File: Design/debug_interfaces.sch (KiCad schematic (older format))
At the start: 2 parts, among them J1 Conn_ARM_JTAG_SWD_10, U4 UART_female

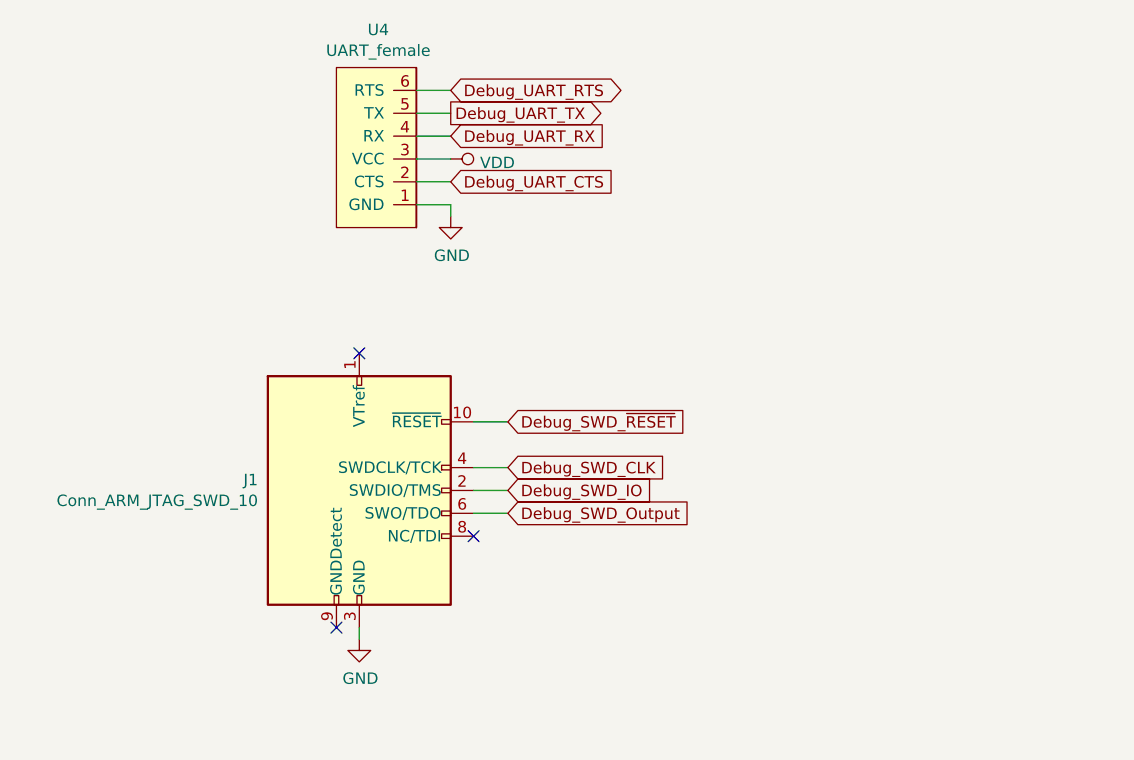
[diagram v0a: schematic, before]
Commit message: Improvement over the Power management: - added TPS6201DRC for raising leaking voltage from supercapacitor - supercap is protected from overvoltage using a shunt diode - power management is using MOSFET logic (2 PFET, 1 NFET)
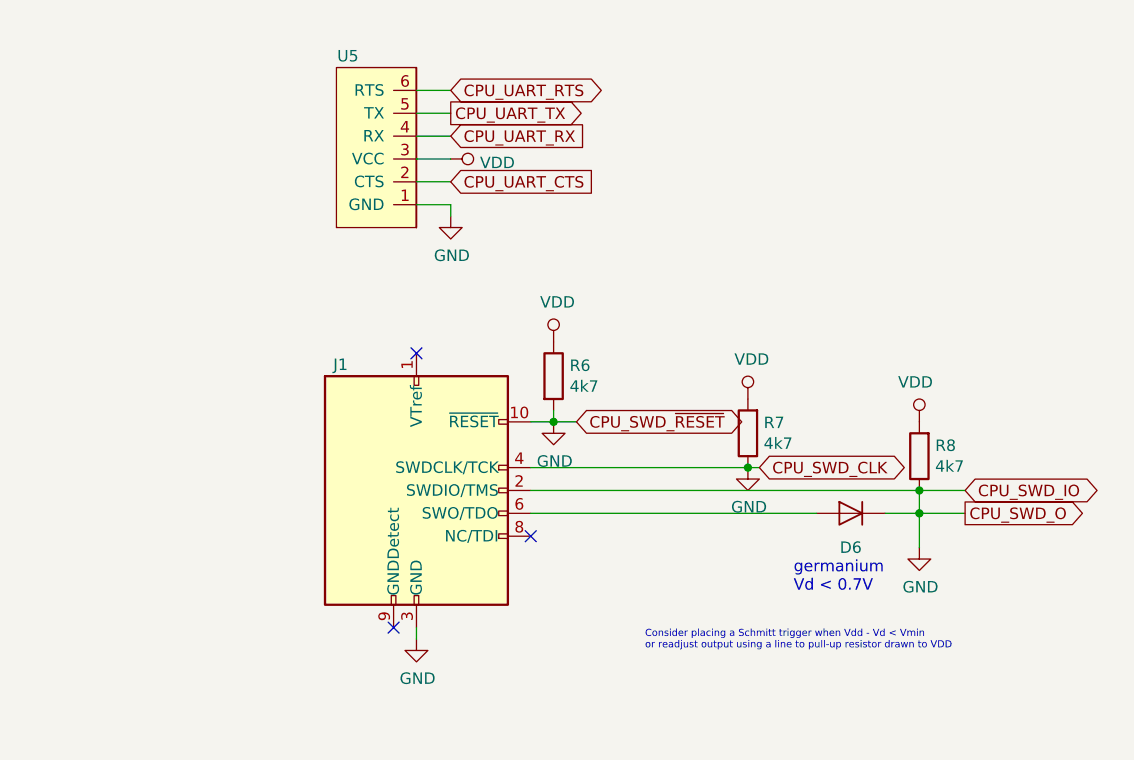
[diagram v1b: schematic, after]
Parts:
- added D6: 1N4148, Diode_THT:D_DO-35_SOD27_P7.62mm_Horizontal, symbol Diode:1N4148
- added R6, R7, R8: 4k7, symbol Device:R
- J1: footprint (none) -> Connector_PinHeader_1.27mm:PinHeader_1x06_P1.27mm_Horizontal
- renumbered U4 to U5
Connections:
- net Debug_SWD_CLK is gone; now on net GND: J1.4 (SWDCLK/TCK)
- net Debug_SWD_IO is gone; now on net GND: J1.2 (SWDIO/TMS)
- net Debug_SWD_~RESET~ is gone; now on net GND: J1.10 (~RESET~)
- net GND: now also D6.1 (K), R6.2, R7.1, R8.1
- net VDD: now also R6.1, R7.2, R8.2
- net Debug_SWD_Output: no longer names the net of J1.6 (SWO/TDO)
- net Debug_SWD_Output: now also D6.2 (A)
- net Debug_UART_CTS renamed CPU_UART_CTS
- net Debug_UART_RTS renamed CPU_UART_RTS
- net Debug_UART_RX renamed CPU_UART_RX
- net Debug_UART_TX renamed CPU_UART_TX
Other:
- note added: "Consider placing a Schmitt trigger when Vdd - Vd < Vmin \nor readjust output using a line to pull-up resistor drawn to VDD"
- note added: "germanium\nVd < 0.7V"
- moved on the sheet: J1
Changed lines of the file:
@@
 L Connector:Conn_ARM_JTAG_SWD_10 J1
 U 1 1 5E1B4BA0
-P 2150 2900
-F 0 "J1" H 1707 2946 50  0000 R CNN
-F 1 "Conn_ARM_JTAG_SWD_10" H 1707 2855 50  0000 R CNN
-F 2 "" H 2150 2900 50  0001 C CNN
-F 3 "http://infocenter.arm.com/help/topic/com.arm.doc.ddi0314h/DDI0314H_coresight_components_trm.pdf" V 1800 1650 50  0001 C CNN
-	1    2150 2900
-	1    0    0    -1
-$EndComp
-$Comp
-L Meishi:UART_female U4
+P 2400 2900
+F 0 "J1" H 2100 3450 50  0000 R CNN
+F 1 "Conn_ARM_JTAG_SWD_10" H 1957 2855 50  0001 R CNN
+F 2 "Connector_PinHeader_1.27mm:PinHeader_1x06_P1.27mm_Horizontal" H 2400 2900 50  0001 C CNN
+F 3 "http://infocenter.arm.com/help/topic/com.arm.doc.ddi0314h/DDI0314H_coresight_components_trm.pdf" V 2050 1650 50  0001 C CNN
+	1    2400 2900
+	1    0    0    -1
+$EndComp
+$Comp
+L Meishi:UART_female U5
 U 1 1 5E1B45D1
 P 2400 1650
-F 0 "U4" H 2567 885 50  0000 C CNN
-F 1 "UART_female" H 2567 976 50  0000 C CNN
+F 0 "U5" H 2700 1000 50  0000 C CNN
+F 1 "UART_female" H 2567 976 50  0001 C CNN
 F 2 "Connector_PinSocket_1.00mm:PinSocket_1x06_P1.00mm_Vertical" H 2800 1100 50  0001 C CNN
 F 3 "" H 2800 1100 50  0001 C CNN
@@
 $EndComp
 $Comp
-L power:GND #PWR0101
+L power:GND #PWR017
 U 1 1 5E1B6C8F
 P 2550 1700
-F 0 "#PWR0101" H 2550 1450 50  0001 C CNN
+F 0 "#PWR017" H 2550 1450 50  0001 C CNN
 F 1 "GND" H 2555 1527 50  0000 C CNN
 F 2 "" H 2550 1700 50  0001 C CNN
@@
 Wire Wire Line
 	2550 1650 2400 1650
-Text GLabel 2550 1250 2    50   Output ~ 0
-Debug_UART_TX
 Wire Wire Line
 	2550 1250 2400 1250
 Text GLabel 2550 1350 2    50   Input ~ 0
-Debug_UART_RX
+CPU_UART_RX
 Wire Wire Line
 	2550 1350 2400 1350
 Text GLabel 2550 1150 2    50   BiDi ~ 0
-Debug_UART_RTS
+CPU_UART_RTS
 Wire Wire Line
 	2550 1150 2400 1150
 Text GLabel 2550 1550 2    50   Input ~ 0
-Debug_UART_CTS
+CPU_UART_CTS
 Wire Wire Line
 	2550 1550 2400 1550
@@
 	2400 1450 2550 1450
 $Comp
-L power:VDD #PWR0102
+L power:VDD #PWR016
 U 1 1 5E1B7012
 P 2550 1450
-F 0 "#PWR0102" H 2550 1300 50  0001 C CNN
+F 0 "#PWR016" H 2550 1300 50  0001 C CNN
 F 1 "VDD" V 2567 1578 50  0000 L CNN
 F 2 "" H 2550 1450 50  0001 C CNN
@@
 $EndComp
 $Comp
-L power:GND #PWR0104
+L power:GND #PWR015
 U 1 1 5E1BD15F
-P 2150 3550
-F 0 "#PWR0104" H 2150 3300 50  0001 C CNN
-F 1 "GND" H 2155 3377 50  0000 C CNN
-F 2 "" H 2150 3550 50  0001 C CNN
-F 3 "" H 2150 3550 50  0001 C CNN
-	1    2150 3550
-	1    0    0    -1
-$EndComp
-Wire Wire Line
-	2150 3550 2150 3500
-Text GLabel 2800 2800 2    50   Input ~ 0
-Debug_SWD_CLK
-Wire Wire Line
-	2800 2800 2650 2800
-Text GLabel 2800 2900 2    50   Input ~ 0
-Debug_SWD_IO
-Text GLabel 2800 3000 2    50   Input ~ 0
-Debug_SWD_Output
-Wire Wire Line
-	2800 2600 2650 2600
-NoConn ~ 2650 3100
-Wire Wire Line
-	2800 3000 2650 3000
-Wire Wire Line
-	2650 2900 2800 2900
-Text GLabel 2800 2600 2    50   Input ~ 0
-Debug_SWD_~RESET~
-NoConn ~ 2150 2300
-NoConn ~ 2050 3500
+P 2400 3550
+F 0 "#PWR015" H 2400 3300 50  0001 C CNN
+F 1 "GND" H 2405 3377 50  0000 C CNN
+F 2 "" H 2400 3550 50  0001 C CNN
+F 3 "" H 2400 3550 50  0001 C CNN
+	1    2400 3550
+	1    0    0    -1
+$EndComp
+Wire Wire Line
+	2400 3550 2400 3500
+NoConn ~ 2900 3100
+NoConn ~ 2400 2300
+NoConn ~ 2300 3500
+Text GLabel 2550 1250 2    50   Output ~ 0
+CPU_UART_TX
+Text GLabel 3100 2600 2    50   BiDi ~ 0
+CPU_SWD_~RESET~
+Text GLabel 3900 2800 2    50   BiDi ~ 0
+CPU_SWD_CLK
+Wire Wire Line
+	2900 2800 3850 2800
+Text GLabel 4800 3000 2    50   Output ~ 0
+CPU_SWD_O
+Text Notes 3400 3600 0    31   ~ 0
+Consider placing a Schmitt trigger when Vdd - Vd < Vmin \nor readjust output using a line to pull-up resistor drawn to VDD
+$Comp
+L Diode:1N4148 D6
+U 1 1 5E2F08DB
+P 4300 3000
+F 0 "D6" H 4300 2850 50  0000 C CNN
+F 1 "1N4148" H 4300 3125 50  0001 C CNN
+F 2 "Diode_THT:D_DO-35_SOD27_P7.62mm_Horizontal" H 4300 2825 50  0001 C CNN
+F 3 "https://assets.nexperia.com/documents/data-sheet/1N4148_1N4448.pdf" H 4300 3000 50  0001 C CNN
+	1    4300 3000
+	-1   0    0    -1
+$EndComp
+$Comp
+L power:VDD #PWR022
+U 1 1 5E61497A
+P 4600 2600
+F 0 "#PWR022" H 4600 2450 50  0001 C CNN
+F 1 "VDD" H 4617 2773 50  0000 C CNN
+F 2 "" H 4600 2600 50  0001 C CNN
+F 3 "" H 4600 2600 50  0001 C CNN
+	1    4600 2600
+	-1   0    0    -1
+$EndComp
+$Comp
+L Device:R R8
+U 1 1 5E615825
+P 4600 2750
+F 0 "R8" H 4531 2704 50  0000 R CNN
+F 1 "4k7" H 4531 2795 50  0000 R CNN
+F 2 "" V 4530 2750 50  0001 C CNN
+F 3 "~" H 4600 2750 50  0001 C CNN
+	1    4600 2750
+	-1   0    0    1
+$EndComp
+$Comp
+L power:GND #PWR023
+U 1 1 5E61DF1C
+P 4600 3150
+F 0 "#PWR023" H 4600 2900 50  0001 C CNN
+F 1 "GND" H 4605 2977 50  0000 C CNN
+F 2 "" H 4600 3150 50  0001 C CNN
+F 3 "" H 4600 3150 50  0001 C CNN
+	1    4600 3150
+	1    0    0    -1
+$EndComp
+Connection ~ 4600 3000
+Wire Wire Line
+	4600 2900 4600 3000
+Wire Wire Line
+	2900 2600 3000 2600
+Wire Wire Line
+	4600 3000 4800 3000
+Wire Wire Line
+	4600 3150 4600 3000
+Text GLabel 4800 2900 2    50   BiDi ~ 0
+CPU_SWD_IO
+Connection ~ 4600 2900
+Wire Wire Line
+	4600 2900 4800 2900
+Wire Wire Line
+	2900 2900 4600 2900
+Wire Wire Line
+	4450 3000 4600 3000
+Wire Wire Line
+	2900 3000 4150 3000
+$Comp
+L power:VDD #PWR018
+U 1 1 5E633191
+P 3000 2250
+F 0 "#PWR018" H 3000 2100 50  0001 C CNN
+F 1 "VDD" H 3017 2423 50  0000 C CNN
+F 2 "" H 3000 2250 50  0001 C CNN
+F 3 "" H 3000 2250 50  0001 C CNN
+	1    3000 2250
+	1    0    0    -1
+$EndComp
+$Comp
+L power:VDD #PWR020
+U 1 1 5E63336E
+P 3850 2500
+F 0 "#PWR020" H 3850 2350 50  0001 C CNN
+F 1 "VDD" H 3867 2673 50  0000 C CNN
+F 2 "" H 3850 2500 50  0001 C CNN
+F 3 "" H 3850 2500 50  0001 C CNN
+	1    3850 2500
+	1    0    0    -1
+$EndComp
+$Comp
+L Device:R R6
+U 1 1 5E6336B6
+P 3000 2400
+F 0 "R6" H 3070 2446 50  0000 L CNN
+F 1 "4k7" H 3070 2355 50  0000 L CNN
+F 2 "" V 2930 2400 50  0001 C CNN
+F 3 "~" H 3000 2400 50  0001 C CNN
+	1    3000 2400
+	1    0    0    -1
+$EndComp
+$Comp
+L Device:R R7
+U 1 1 5E633EAA
+P 3850 2650
+F 0 "R7" H 3781 2604 50  0000 R CNN
+F 1 "4k7" H 3781 2695 50  0000 R CNN
+F 2 "" V 3780 2650 50  0001 C CNN
+F 3 "~" H 3850 2650 50  0001 C CNN
+	1    3850 2650
+	-1   0    0    1
+$EndComp
+Wire Wire Line
+	3000 2550 3000 2600
+Connection ~ 3000 2600
+Wire Wire Line
+	3000 2600 3100 2600
+Connection ~ 3850 2800
+Wire Wire Line
+	3850 2800 3900 2800
+$Comp
+L power:GND #PWR019
+U 1 1 5E63643E
+P 3000 2600
+F 0 "#PWR019" H 3000 2350 50  0001 C CNN
+F 1 "GND" H 3005 2427 50  0000 C CNN
+F 2 "" H 3000 2600 50  0001 C CNN
+F 3 "" H 3000 2600 50  0001 C CNN
+	1    3000 2600
+	1    0    0    -1
+$EndComp
+$Comp
+L power:GND #PWR021
+U 1 1 5E636AB3
+P 3850 2800
+F 0 "#PWR021" H 3850 2550 50  0001 C CNN
+F 1 "GND" H 3855 2627 50  0000 C CNN
+F 2 "" H 3850 2800 50  0001 C CNN
+F 3 "" H 3850 2800 50  0001 C CNN
+	1    3850 2800
+	1    0    0    -1
+$EndComp
+Text Notes 4050 3350 0    50   ~ 0
+germanium\nVd < 0.7V
 $EndSCHEMATC

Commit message: - designed configurable intensity for RGB LEDs - included Breakout (FET, Diode, etc.) Spice models from Cadence Spice - replaced global label with hierarchical complete view - customized net labels with pin function - exported first spice netlist which presents small bugs
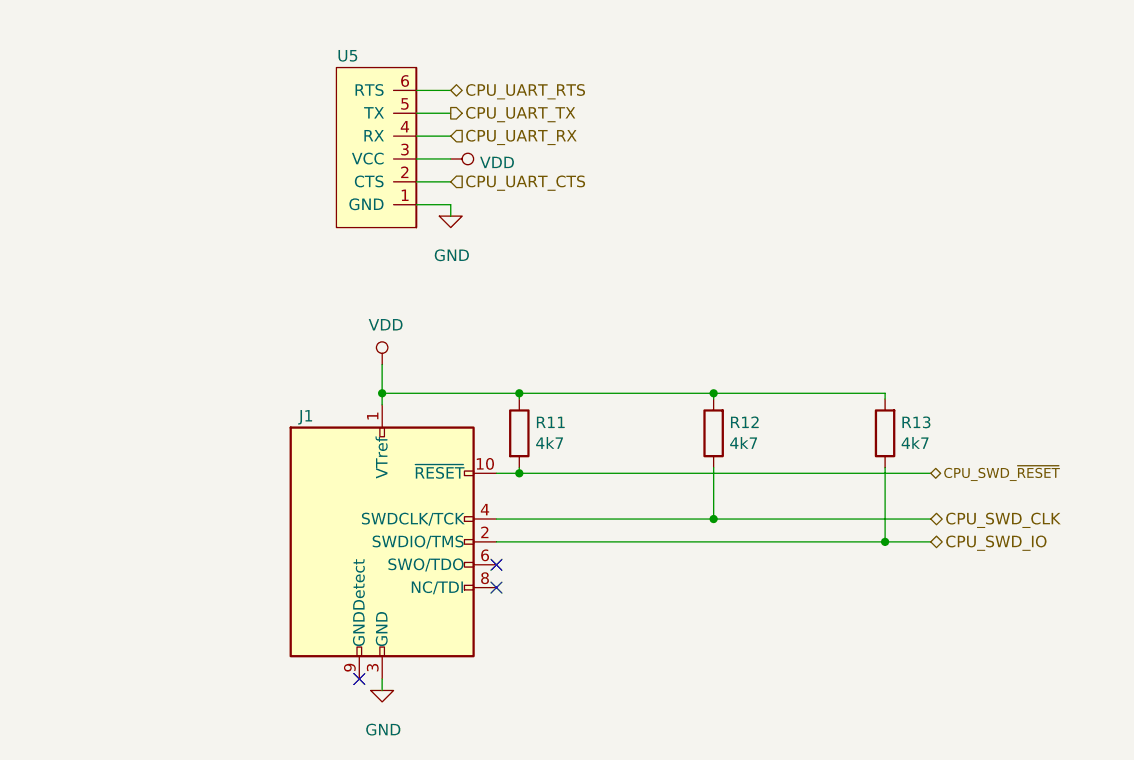
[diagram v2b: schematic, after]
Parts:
- removed D6: 1N4148, Diode_THT:D_DO-35_SOD27_P7.62mm_Horizontal, symbol Diode:1N4148
- renumbered R6 to R11, R7 to R12, R8 to R13
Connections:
- net VDD: now also J1.1 (VTref)
- removed net GND: J1.10 (~RESET~), J1.2 (SWDIO/TMS), J1.3 (GND), J1.4 (SWDCLK/TCK), J1.5 (GND), R11.2, R12.1, R13.1, U5.1 (GND)
- new net 0: J1.3 (GND), J1.5 (GND), U5.1 (GND)
- new net CPU_SWD_CLK: J1.4 (SWDCLK/TCK), R12.1
- new net CPU_SWD_IO: J1.2 (SWDIO/TMS), R13.1
- new net CPU_SWD_~RESET~: J1.10 (~RESET~), R11.2
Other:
- note removed: "Consider placing a Schmitt trigger when Vdd - Vd < Vmin \nor readjust output using a line to pull-up resistor drawn to VDD"
- note removed: "germanium\nVd < 0.7V"
- moved on the sheet: J1, R11, R12, R13
